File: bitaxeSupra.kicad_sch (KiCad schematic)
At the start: 20 parts, among them J1 PJ-036AH-SMT

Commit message: bm1366 sheet renamed to bm1368
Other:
- sheet BM1366 renamed BM1368
- sheet BM1368: file bm1366.kicad_sch -> bm1368.kicad_sch
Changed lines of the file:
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@@
     )
     (instances
-      (project "bitaxeUltra"
+      (project "bitaxeSupra"
         (path "/e63e39d7-6ac0-4ffd-8aa3-1841a4541b55"
           (reference "FID2") (unit 1)
@@
     )
     (instances
-      (project "bitaxeUltra"
+      (project "bitaxeSupra"
         (path "/e63e39d7-6ac0-4ffd-8aa3-1841a4541b55"
           (reference "FID3") (unit 1)
@@
     )
     (instances
-      (project "bitaxeUltra"
+      (project "bitaxeSupra"
         (path "/e63e39d7-6ac0-4ffd-8aa3-1841a4541b55"
           (reference "FID4") (unit 1)
@@
     )
     (instances
-      (project "bitaxeUltra"
+      (project "bitaxeSupra"
         (path "/e63e39d7-6ac0-4ffd-8aa3-1841a4541b55"
           (reference "FID6") (unit 1)
@@
     (pin "1")
     (instances
-      (project "bitaxeUltra"
+      (project "bitaxeSupra"
         (path "/e63e39d7-6ac0-4ffd-8aa3-1841a4541b55/4cf9c075-d009-4c35-9949-adda70ae20c7"
           (reference "TP7") (unit 1)
@@
     (pin "1")
     (instances
-      (project "bitaxeUltra"
+      (project "bitaxeSupra"
         (path "/e63e39d7-6ac0-4ffd-8aa3-1841a4541b55/4cf9c075-d009-4c35-9949-adda70ae20c7"
           (reference "TP7") (unit 1)
@@
     )
     (instances
-      (project "bitaxeUltra"
+      (project "bitaxeSupra"
         (path "/e63e39d7-6ac0-4ffd-8aa3-1841a4541b55"
           (reference "H2") (unit 1)
@@
     (pin "3")
     (instances
-      (project "bitaxeUltra"
+      (project "bitaxeSupra"
         (path "/e63e39d7-6ac0-4ffd-8aa3-1841a4541b55"
           (reference "J1") (unit 1)
@@
     (pin "1")
     (instances
-      (project "bitaxeUltra"
+      (project "bitaxeSupra"
         (path "/e63e39d7-6ac0-4ffd-8aa3-1841a4541b55"
           (reference "H7") (unit 1)
@@
     )
     (instances
-      (project "bitaxeUltra"
+      (project "bitaxeSupra"
         (path "/e63e39d7-6ac0-4ffd-8aa3-1841a4541b55"
           (reference "H1") (unit 1)
@@
     )
     (instances
-      (project "bitaxeUltra"
+      (project "bitaxeSupra"
         (path "/e63e39d7-6ac0-4ffd-8aa3-1841a4541b55"
           (reference "FID1") (unit 1)
@@
     )
     (instances
-      (project "bitaxeUltra"
+      (project "bitaxeSupra"
         (path "/e63e39d7-6ac0-4ffd-8aa3-1841a4541b55"
           (reference "FID8") (unit 1)
@@
     )
     (instances
-      (project "bitaxeUltra"
+      (project "bitaxeSupra"
         (path "/e63e39d7-6ac0-4ffd-8aa3-1841a4541b55"
           (reference "FID5") (unit 1)
@@
     )
     (instances
-      (project "bitaxeUltra"
+      (project "bitaxeSupra"
         (path "/e63e39d7-6ac0-4ffd-8aa3-1841a4541b55"
           (reference "H6") (unit 1)
@@
     )
     (instances
-      (project "bitaxeUltra"
+      (project "bitaxeSupra"
         (path "/e63e39d7-6ac0-4ffd-8aa3-1841a4541b55"
           (reference "FID7") (unit 1)
@@
     )
     (instances
-      (project "bitaxeUltra"
+      (project "bitaxeSupra"
         (path "/e63e39d7-6ac0-4ffd-8aa3-1841a4541b55"
           (reference "H5") (unit 1)
@@
     (pin "1")
     (instances
-      (project "bitaxeUltra"
+      (project "bitaxeSupra"
         (path "/e63e39d7-6ac0-4ffd-8aa3-1841a4541b55"
           (reference "H9") (unit 1)
@@
     (pin "1")
     (instances
-      (project "bitaxeUltra"
+      (project "bitaxeSupra"
         (path "/e63e39d7-6ac0-4ffd-8aa3-1841a4541b55"
           (reference "H8") (unit 1)
@@
     (pin "1")
     (instances
-      (project "bitaxeUltra"
+      (project "bitaxeSupra"
         (path "/e63e39d7-6ac0-4ffd-8aa3-1841a4541b55"
           (reference "H10") (unit 1)
@@
     )
     (instances
-      (project "bitaxeUltra"
+      (project "bitaxeSupra"
         (path "/e63e39d7-6ac0-4ffd-8aa3-1841a4541b55"
           (reference "#G1") (unit 1)
@@
     )
     (instances
-      (project "bitaxeUltra"
+      (project "bitaxeSupra"
         (path "/e63e39d7-6ac0-4ffd-8aa3-1841a4541b55"
           (reference "U3") (unit 1)
@@
     (stroke (width 0.1524) (type solid))
     (fill (color 255 255 194 1.0000))
-    (property "Sheetname" "BM1366" (at 112.395 66.5984 0)
+    (property "Sheetname" "BM1368" (at 112.395 66.5984 0)
       (effects (font (size 1.27 1.27)) (justify left bottom))
     )
-    (property "Sheetfile" "bm1366.kicad_sch" (at 112.395 83.7696 0)
+    (property "Sheetfile" "bm1368.kicad_sch" (at 112.395 83.7696 0)
       (effects (font (size 1.27 1.27)) (justify left top))
     )
@@
     )
     (instances
-      (project "bitaxeUltra"
+      (project "bitaxeSupra"
         (path "/e63e39d7-6ac0-4ffd-8aa3-1841a4541b55" (page "4"))
       )
@@
     )
     (instances
-      (project "bitaxeUltra"
+      (project "bitaxeSupra"
         (path "/e63e39d7-6ac0-4ffd-8aa3-1841a4541b55" (page "5"))
       )
@@
     )
     (instances
-      (project "bitaxeUltra"
+      (project "bitaxeSupra"
         (path "/e63e39d7-6ac0-4ffd-8aa3-1841a4541b55" (page "2"))
       )
@@
     )
     (instances
-      (project "bitaxeUltra"
+      (project "bitaxeSupra"
         (path "/e63e39d7-6ac0-4ffd-8aa3-1841a4541b55" (page "3"))
       )

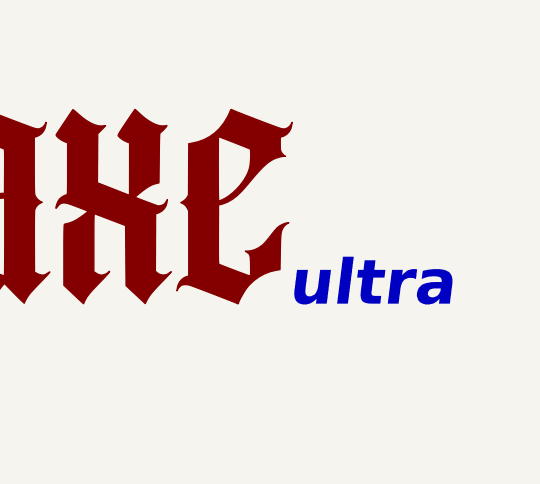
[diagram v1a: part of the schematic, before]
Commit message: schematic title update
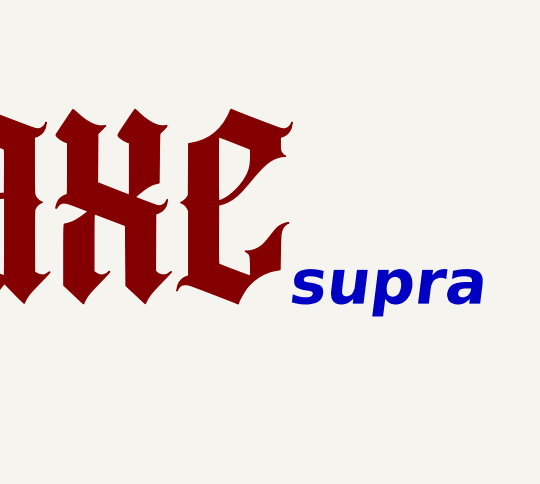
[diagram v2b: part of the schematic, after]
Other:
- note added: "supra"
- note removed: "ultra"
- title: Bitaxe Ultra -> Bitaxe Supra
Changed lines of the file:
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@@
   (paper "A")
   (title_block
-    (title "Bitaxe Ultra")
-    (date "2023-12-15")
-    (rev "205")
+    (title "Bitaxe Supra")
+    (date "2024-02-14")
+    (rev "401")
   )
   (junction (at 208.915 69.85) (diameter 0) (color 0 0 0 0)
@@
     (stroke (width 0) (type default))
   )
-  (text "ultra" (at 235.585 186.055 0)
+  (text "supra" (at 235.585 186.055 0)
     (effects (font (size 5 5) (thickness 1) bold italic) (justify left bottom))
   )

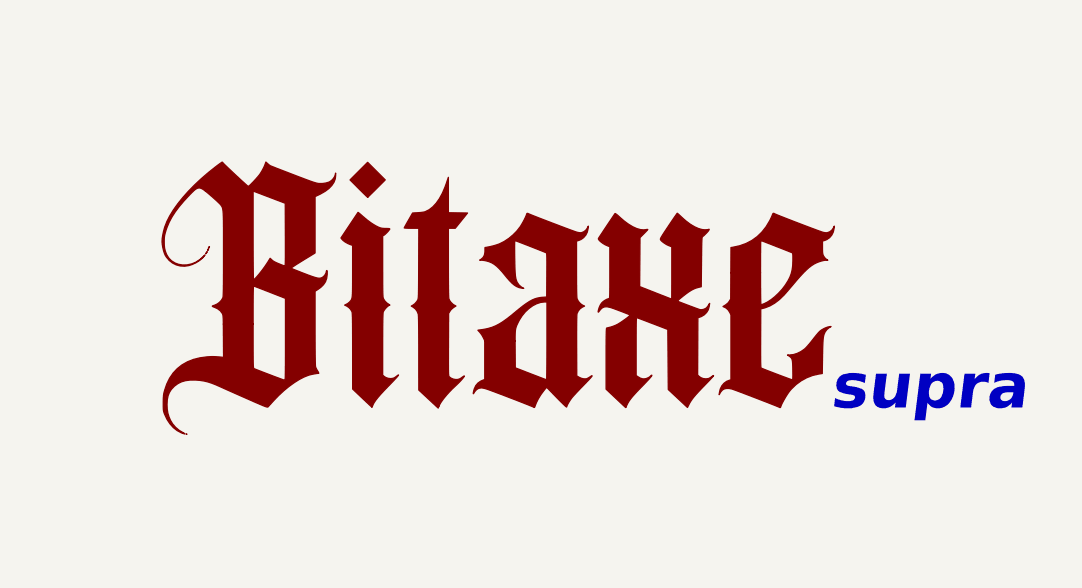
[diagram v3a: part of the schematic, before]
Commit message: track cleanup, added BOM
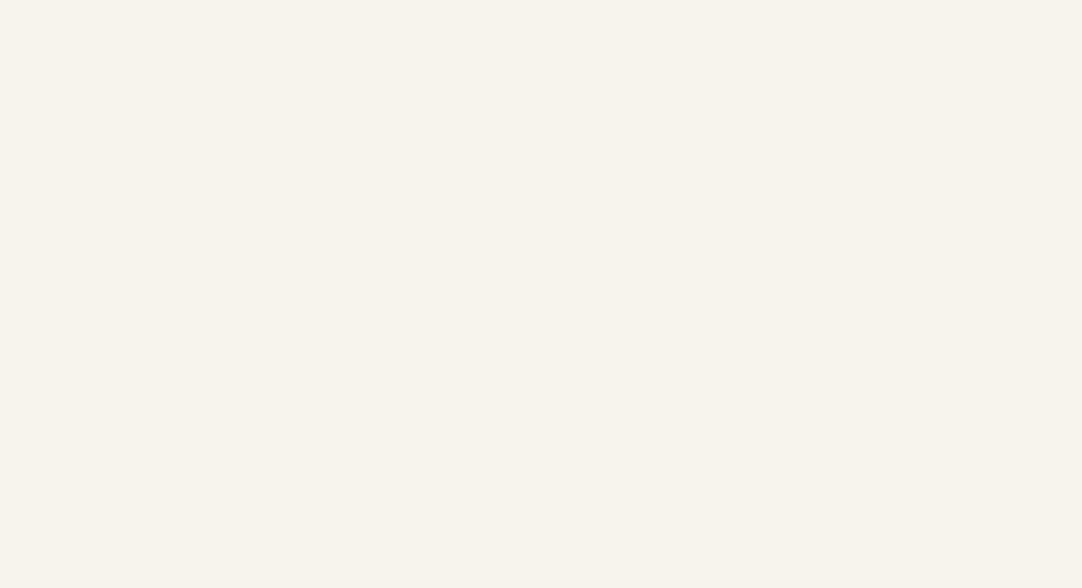
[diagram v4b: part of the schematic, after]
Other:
- note removed: "supra"
- title: Bitaxe Supra -> bitaxeSupra
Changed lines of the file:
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@@
   (paper "A")
   (title_block
-    (title "Bitaxe Supra")
+    (title "bitaxeSupra")
     (date "2024-02-14")
     (rev "401")
@@
   (wire (pts (xy 129.54 43.815) (xy 137.16 43.815))
     (stroke (width 0) (type default))
-  )
-  (text "supra" (at 235.585 186.055 0)
-    (effects (font (size 5 5) (thickness 1) bold italic) (justify left bottom))
   )
   (label "PLUG_SENSE" (at 90.805 45.72 180) (fields_autoplaced)
@@
         )
       )
-    )
-  )
-  (symbol (lib_id "bitaxe:LOGO") (at 197.485 173.99 0) (unit 1)
-    (in_bom yes) (on_board yes) (dnp no) (fields_autoplaced)
-    (property "Reference" "#G1" (at 197.485 146.4607 0)
-      (effects (font (size 1.27 1.27)) hide)
-    )
-    (property "Value" "LOGO" (at 197.485 201.5193 0)
-      (effects (font (size 1.27 1.27)) hide)
-    )
-    (property "Footprint" "" (at 197.485 173.99 0)
-      (effects (font (size 1.27 1.27)) hide)
-    )
-    (property "Datasheet" "" (at 197.485 173.99 0)
-      (effects (font (size 1.27 1.27)) hide)
-    )
-    (instances
-      (project "bitaxeSupra"
-        (path "/e63e39d7-6ac0-4ffd-8aa3-1841a4541b55"
-          (reference "#G1") (unit 1)
-        )
-      )

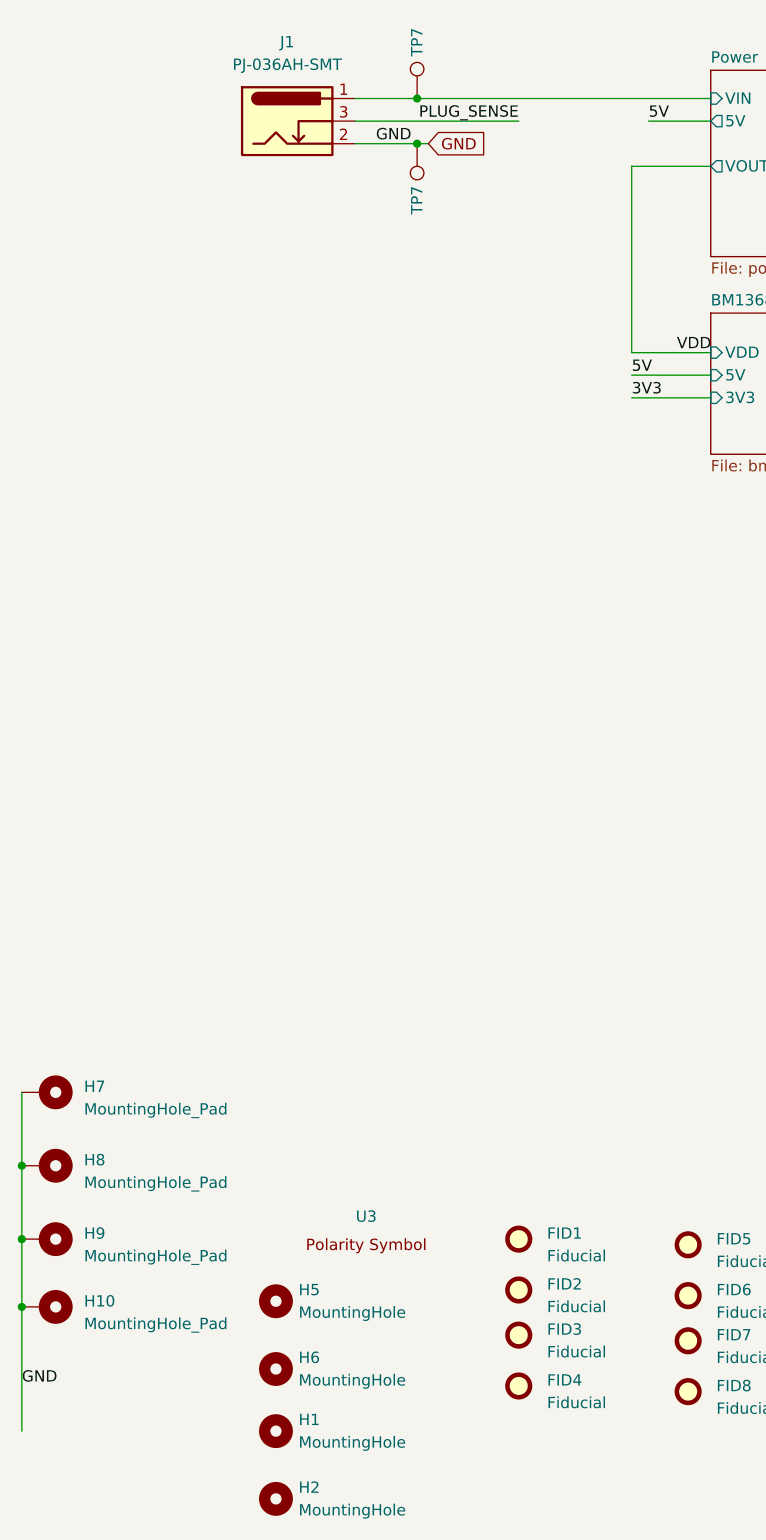
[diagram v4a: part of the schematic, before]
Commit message: update to KiCad8, DNP 32KHz crystal, update BOM
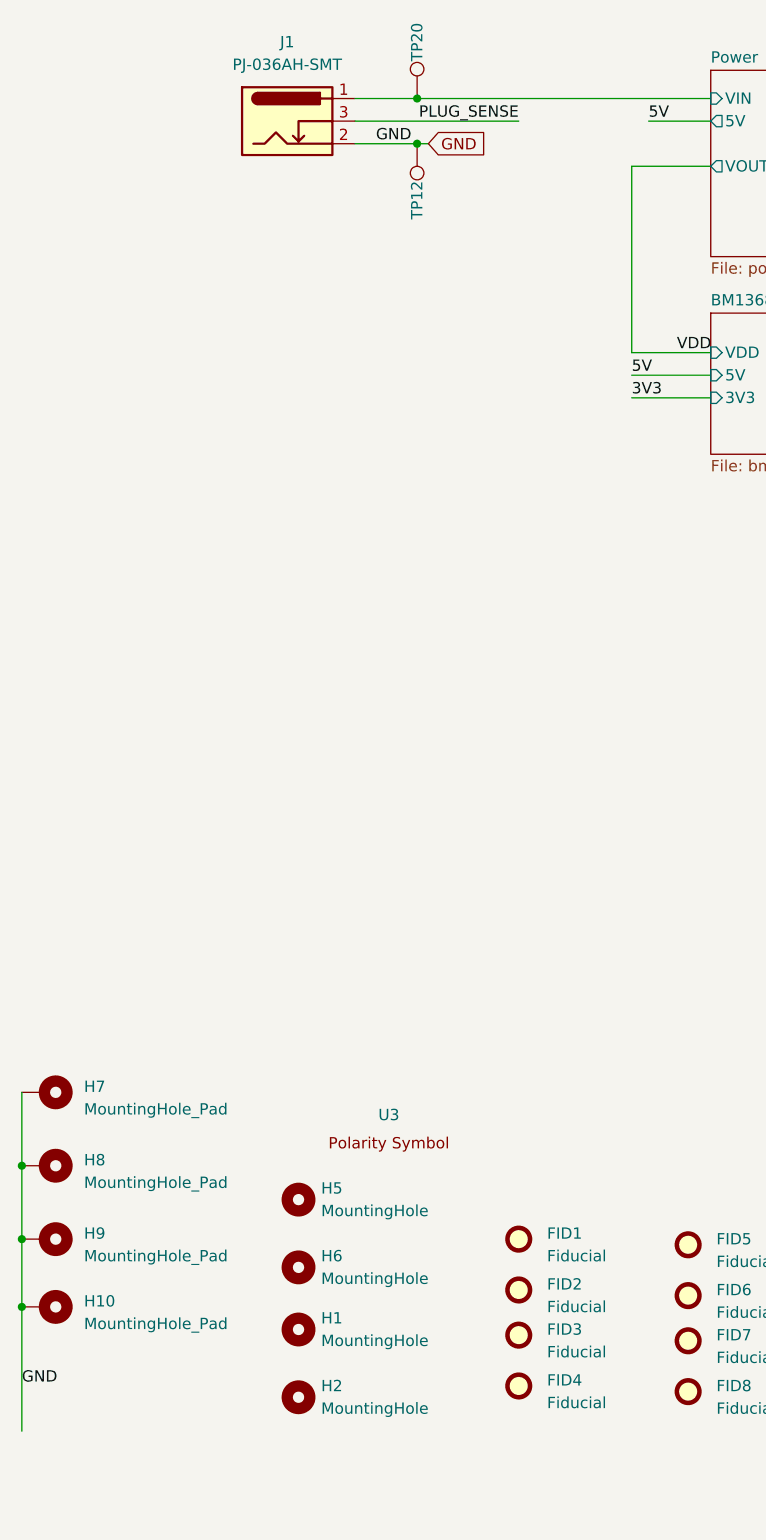
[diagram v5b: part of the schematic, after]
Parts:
- renumbered TP7 to TP12, TP7 to TP20
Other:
- moved on the sheet: H1, H2, H5, H6, U3
